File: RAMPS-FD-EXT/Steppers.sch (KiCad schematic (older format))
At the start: 20 parts, among them P401 CONN_3X2, P402 CONN_3X2, P403 MOT_0, P404 MOT_1, P405 CONN_3X2, P406 CONN_3X2, P407 MOT_3, P408 MOT_2, U401 Stepper0, U402 Stepper1, U403 Stepper3, U404 Stepper2

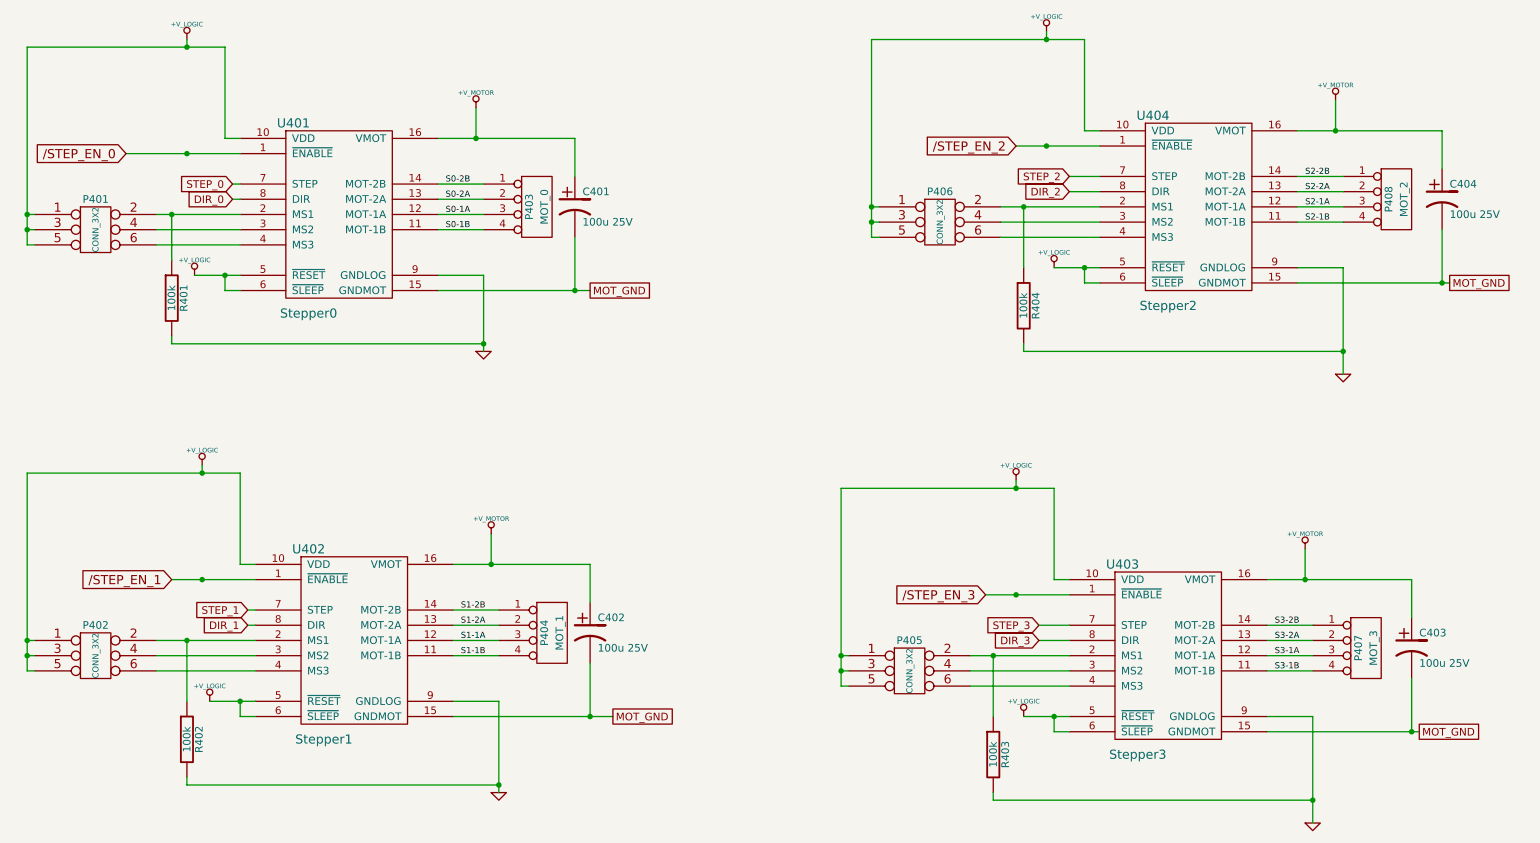
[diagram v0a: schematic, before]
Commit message: EXT4: update schematic, layout
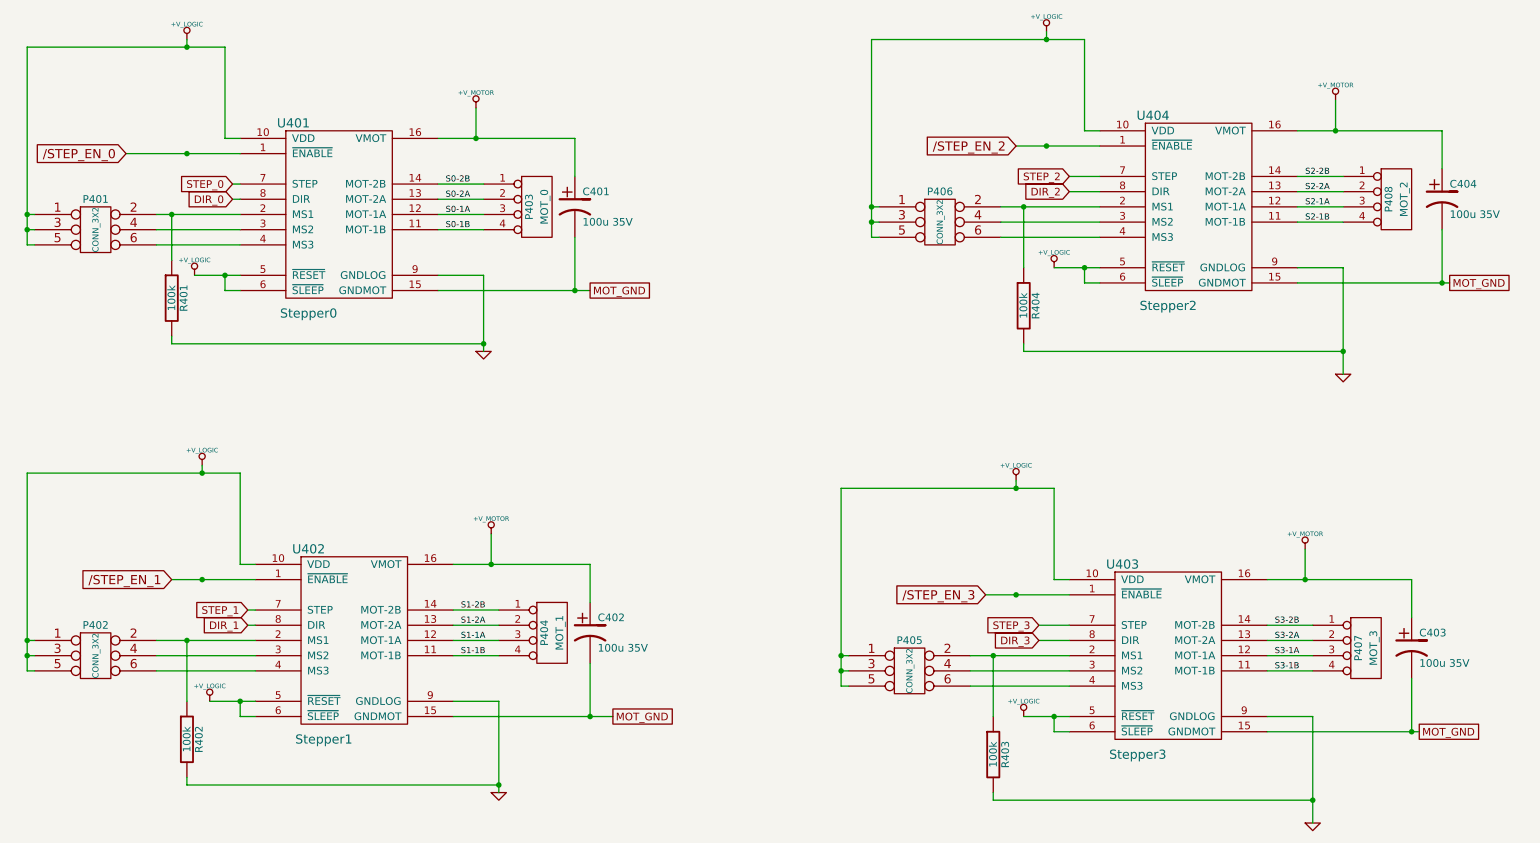
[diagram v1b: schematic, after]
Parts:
- C401, C402, C403, C404: value 100u 25V -> 100u 35V
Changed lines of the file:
@@
 Sheet 4 4
 Title ""
-Date "21 sep 2013"
+Date "26 sep 2013"
 Rev ""
 Comp ""
@@
 MOT_GND
 $Comp
-L +V_LOGIC #PWR054
+L +V_LOGIC #PWR058
 U 1 1 523B891F
 P 7500 5450
-F 0 "#PWR054" H 7500 5420 30  0001 C CNN
+F 0 "#PWR058" H 7500 5420 30  0001 C CNN
 F 1 "+V_LOGIC" H 7500 5550 30  0000 C CNN
 F 2 "" H 7500 5450 60  0001 C CNN
@@
 $EndComp
 $Comp
-L +V_LOGIC #PWR055
+L +V_LOGIC #PWR059
 U 1 1 523B891E
 P 7450 3900
-F 0 "#PWR055" H 7450 3870 30  0001 C CNN
+F 0 "#PWR059" H 7450 3870 30  0001 C CNN
 F 1 "+V_LOGIC" H 7450 4000 30  0000 C CNN
 F 2 "" H 7450 3900 60  0001 C CNN
@@
 $EndComp
 $Comp
-L +V_MOTOR #PWR056
+L +V_MOTOR #PWR060
 U 1 1 523B891D
 P 9350 4350
-F 0 "#PWR056" H 9350 4320 30  0001 C CNN
+F 0 "#PWR060" H 9350 4320 30  0001 C CNN
 F 1 "+V_MOTOR" H 9350 4450 30  0000 C CNN
 F 2 "" H 9350 4350 60  0001 C CNN
@@
 P 10050 5000
 F 0 "C403" H 10100 5100 50  0000 L CNN
-F 1 "100u 25V" H 10100 4900 50  0000 L CNN
+F 1 "100u 35V" H 10100 4900 50  0000 L CNN
 F 2 "" H 10050 5000 60  0001 C CNN
 F 3 "" H 10050 5000 60  0001 C CNN
@@
 $EndComp
 $Comp
-L GND #PWR057
+L GND #PWR061
 U 1 1 523B8918
 P 9400 6150
-F 0 "#PWR057" H 9400 6150 30  0001 C CNN
+F 0 "#PWR061" H 9400 6150 30  0001 C CNN
 F 1 "GND" H 9400 6080 30  0001 C CNN
 F 2 "" H 9400 6150 60  0001 C CNN
@@
 $EndComp
 $Comp
-L GND #PWR058
+L GND #PWR062
 U 1 1 523B869B
 P 9600 3200
-F 0 "#PWR058" H 9600 3200 30  0001 C CNN
+F 0 "#PWR062" H 9600 3200 30  0001 C CNN
 F 1 "GND" H 9600 3130 30  0001 C CNN
 F 2 "" H 9600 3200 60  0001 C CNN
@@
 P 4550 2100
 F 0 "C401" H 4600 2200 50  0000 L CNN
-F 1 "100u 25V" H 4600 2000 50  0000 L CNN
+F 1 "100u 35V" H 4600 2000 50  0000 L CNN
 F 2 "" H 4550 2100 60  0001 C CNN
 F 3 "" H 4550 2100 60  0001 C CNN
@@
 P 4650 4900
 F 0 "C402" H 4700 5000 50  0000 L CNN
-F 1 "100u 25V" H 4700 4800 50  0000 L CNN
+F 1 "100u 35V" H 4700 4800 50  0000 L CNN
 F 2 "" H 4650 4900 60  0001 C CNN
 F 3 "" H 4650 4900 60  0001 C CNN
@@
 P 10250 2050
 F 0 "C404" H 10300 2150 50  0000 L CNN
-F 1 "100u 25V" H 10300 1950 50  0000 L CNN
+F 1 "100u 35V" H 10300 1950 50  0000 L CNN
 F 2 "" H 10250 2050 60  0001 C CNN
 F 3 "" H 10250 2050 60  0001 C CNN
@@
 $EndComp
 $Comp
-L GND #PWR059
+L GND #PWR063
 U 1 1 523B8694
 P 3950 3050
-F 0 "#PWR059" H 3950 3050 30  0001 C CNN
+F 0 "#PWR063" H 3950 3050 30  0001 C CNN
 F 1 "GND" H 3950 2980 30  0001 C CNN
 F 2 "" H 3950 3050 60  0001 C CNN
@@
 $EndComp
 $Comp
-L GND #PWR060
+L GND #PWR064
 U 1 1 523B8693
 P 4050 5950
-F 0 "#PWR060" H 4050 5950 30  0001 C CNN
+F 0 "#PWR064" H 4050 5950 30  0001 C CNN
 F 1 "GND" H 4050 5880 30  0001 C CNN
 F 2 "" H 4050 5950 60  0001 C CNN
@@
 $EndComp
 $Comp
-L +V_MOTOR #PWR061
+L +V_MOTOR #PWR065
 U 1 1 523B8690
 P 3900 1450
-F 0 "#PWR061" H 3900 1420 30  0001 C CNN
+F 0 "#PWR065" H 3900 1420 30  0001 C CNN
 F 1 "+V_MOTOR" H 3900 1550 30  0000 C CNN
 F 2 "" H 3900 1450 60  0001 C CNN
@@
 $EndComp
 $Comp
-L +V_MOTOR #PWR062
+L +V_MOTOR #PWR066
 U 1 1 523B868F
 P 4000 4250
-F 0 "#PWR062" H 4000 4220 30  0001 C CNN
+F 0 "#PWR066" H 4000 4220 30  0001 C CNN
 F 1 "+V_MOTOR" H 4000 4350 30  0000 C CNN
 F 2 "" H 4000 4250 60  0001 C CNN
@@
 $EndComp
 $Comp
-L +V_MOTOR #PWR063
+L +V_MOTOR #PWR067
 U 1 1 523B868E
 P 9550 1400
-F 0 "#PWR063" H 9550 1370 30  0001 C CNN
+F 0 "#PWR067" H 9550 1370 30  0001 C CNN
 F 1 "+V_MOTOR" H 9550 1500 30  0000 C CNN
 F 2 "" H 9550 1400 60  0001 C CNN
@@
 $EndComp
 $Comp
-L +V_LOGIC #PWR064
+L +V_LOGIC #PWR068
 U 1 1 523B868D
 P 2000 1000
-F 0 "#PWR064" H 2000 970 30  0001 C CNN
+F 0 "#PWR068" H 2000 970 30  0001 C CNN
 F 1 "+V_LOGIC" H 2000 1100 30  0000 C CNN
 F 2 "" H 2000 1000 60  0001 C CNN
@@
 $EndComp
 $Comp
-L +V_LOGIC #PWR065
+L +V_LOGIC #PWR069
 U 1 1 523B868C
 P 2100 3800
-F 0 "#PWR065" H 2100 3770 30  0001 C CNN
+F 0 "#PWR069" H 2100 3770 30  0001 C CNN
 F 1 "+V_LOGIC" H 2100 3900 30  0000 C CNN
 F 2 "" H 2100 3800 60  0001 C CNN
@@
 $EndComp
 $Comp
-L +V_LOGIC #PWR066
+L +V_LOGIC #PWR070
 U 1 1 523B868B
 P 7650 950
-F 0 "#PWR066" H 7650 920 30  0001 C CNN
+F 0 "#PWR070" H 7650 920 30  0001 C CNN
 F 1 "+V_LOGIC" H 7650 1050 30  0000 C CNN
 F 2 "" H 7650 950 60  0001 C CNN
@@
 $EndComp
 $Comp
-L +V_LOGIC #PWR067
+L +V_LOGIC #PWR071
 U 1 1 523B868A
 P 2050 2550
-F 0 "#PWR067" H 2050 2520 30  0001 C CNN
+F 0 "#PWR071" H 2050 2520 30  0001 C CNN
 F 1 "+V_LOGIC" H 2050 2650 30  0000 C CNN
 F 2 "" H 2050 2550 60  0001 C CNN
@@
 $EndComp
 $Comp
-L +V_LOGIC #PWR068
+L +V_LOGIC #PWR072
 U 1 1 523B8689
 P 2150 5350
-F 0 "#PWR068" H 2150 5320 30  0001 C CNN
+F 0 "#PWR072" H 2150 5320 30  0001 C CNN
 F 1 "+V_LOGIC" H 2150 5450 30  0000 C CNN
 F 2 "" H 2150 5350 60  0001 C CNN
@@
 $EndComp
 $Comp
-L +V_LOGIC #PWR069
+L +V_LOGIC #PWR073
 U 1 1 523B8688
 P 7700 2500
-F 0 "#PWR069" H 7700 2470 30  0001 C CNN
+F 0 "#PWR073" H 7700 2470 30  0001 C CNN
 F 1 "+V_LOGIC" H 7700 2600 30  0000 C CNN
 F 2 "" H 7700 2500 60  0001 C CNN

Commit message: RAMPS-FD-EXT: update, schematic, routing and gerbers
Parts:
- P401: value CONN_3X2 -> M0
- P402: value CONN_3X2 -> M1
- P405: value CONN_3X2 -> M3
- P406: value CONN_3X2 -> M2
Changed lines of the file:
@@
 Sheet 4 4
 Title ""
-Date "26 sep 2013"
+Date "6 oct 2013"
 Rev ""
 Comp ""
@@
 MOT_GND
 $Comp
-L +V_LOGIC #PWR058
+L +V_LOGIC #PWR059
 U 1 1 523B891F
 P 7500 5450
-F 0 "#PWR058" H 7500 5420 30  0001 C CNN
+F 0 "#PWR059" H 7500 5420 30  0001 C CNN
 F 1 "+V_LOGIC" H 7500 5550 30  0000 C CNN
 F 2 "" H 7500 5450 60  0001 C CNN
@@
 $EndComp
 $Comp
-L +V_LOGIC #PWR059
+L +V_LOGIC #PWR060
 U 1 1 523B891E
 P 7450 3900
-F 0 "#PWR059" H 7450 3870 30  0001 C CNN
+F 0 "#PWR060" H 7450 3870 30  0001 C CNN
 F 1 "+V_LOGIC" H 7450 4000 30  0000 C CNN
 F 2 "" H 7450 3900 60  0001 C CNN
@@
 $EndComp
 $Comp
-L +V_MOTOR #PWR060
+L +V_MOTOR #PWR061
 U 1 1 523B891D
 P 9350 4350
-F 0 "#PWR060" H 9350 4320 30  0001 C CNN
+F 0 "#PWR061" H 9350 4320 30  0001 C CNN
 F 1 "+V_MOTOR" H 9350 4450 30  0000 C CNN
 F 2 "" H 9350 4350 60  0001 C CNN
@@
 P 6750 5200
 F 0 "P405" H 6750 5450 50  0000 C CNN
-F 1 "CONN_3X2" V 6750 5250 40  0000 C CNN
+F 1 "M3" V 6750 5250 40  0000 C CNN
 F 2 "" H 6750 5200 60  0001 C CNN
 F 3 "" H 6750 5200 60  0001 C CNN
@@
 $EndComp
 $Comp
-L GND #PWR061
+L GND #PWR062
 U 1 1 523B8918
 P 9400 6150
-F 0 "#PWR061" H 9400 6150 30  0001 C CNN
+F 0 "#PWR062" H 9400 6150 30  0001 C CNN
 F 1 "GND" H 9400 6080 30  0001 C CNN
 F 2 "" H 9400 6150 60  0001 C CNN
@@
 P 1400 2300
 F 0 "P401" H 1400 2550 50  0000 C CNN
-F 1 "CONN_3X2" V 1400 2350 40  0000 C CNN
+F 1 "M0" V 1400 2350 40  0000 C CNN
 F 2 "" H 1400 2300 60  0001 C CNN
 F 3 "" H 1400 2300 60  0001 C CNN
@@
 P 1400 5100
 F 0 "P402" H 1400 5350 50  0000 C CNN
-F 1 "CONN_3X2" V 1400 5150 40  0000 C CNN
+F 1 "M1" V 1400 5150 40  0000 C CNN
 F 2 "" H 1400 5100 60  0001 C CNN
 F 3 "" H 1400 5100 60  0001 C CNN
@@
 $EndComp
 $Comp
-L GND #PWR062
+L GND #PWR063
 U 1 1 523B869B
 P 9600 3200
-F 0 "#PWR062" H 9600 3200 30  0001 C CNN
+F 0 "#PWR063" H 9600 3200 30  0001 C CNN
 F 1 "GND" H 9600 3130 30  0001 C CNN
 F 2 "" H 9600 3200 60  0001 C CNN
@@
 P 6950 2250
 F 0 "P406" H 6950 2500 50  0000 C CNN
-F 1 "CONN_3X2" V 6950 2300 40  0000 C CNN
+F 1 "M2" V 6950 2300 40  0000 C CNN
 F 2 "" H 6950 2250 60  0001 C CNN
 F 3 "" H 6950 2250 60  0001 C CNN
@@
 $EndComp
 $Comp
-L GND #PWR063
+L GND #PWR064
 U 1 1 523B8694
 P 3950 3050
-F 0 "#PWR063" H 3950 3050 30  0001 C CNN
+F 0 "#PWR064" H 3950 3050 30  0001 C CNN
 F 1 "GND" H 3950 2980 30  0001 C CNN
 F 2 "" H 3950 3050 60  0001 C CNN
@@
 $EndComp
 $Comp
-L GND #PWR064
+L GND #PWR065
 U 1 1 523B8693
 P 4050 5950
-F 0 "#PWR064" H 4050 5950 30  0001 C CNN
+F 0 "#PWR065" H 4050 5950 30  0001 C CNN
 F 1 "GND" H 4050 5880 30  0001 C CNN
 F 2 "" H 4050 5950 60  0001 C CNN
@@
 $EndComp
 $Comp
-L +V_MOTOR #PWR065
+L +V_MOTOR #PWR066
 U 1 1 523B8690
 P 3900 1450
-F 0 "#PWR065" H 3900 1420 30  0001 C CNN
+F 0 "#PWR066" H 3900 1420 30  0001 C CNN
 F 1 "+V_MOTOR" H 3900 1550 30  0000 C CNN
 F 2 "" H 3900 1450 60  0001 C CNN
@@
 $EndComp
 $Comp
-L +V_MOTOR #PWR066
+L +V_MOTOR #PWR067
 U 1 1 523B868F
 P 4000 4250
-F 0 "#PWR066" H 4000 4220 30  0001 C CNN
+F 0 "#PWR067" H 4000 4220 30  0001 C CNN
 F 1 "+V_MOTOR" H 4000 4350 30  0000 C CNN
 F 2 "" H 4000 4250 60  0001 C CNN
@@
 $EndComp
 $Comp
-L +V_MOTOR #PWR067
+L +V_MOTOR #PWR068
 U 1 1 523B868E
 P 9550 1400
-F 0 "#PWR067" H 9550 1370 30  0001 C CNN
+F 0 "#PWR068" H 9550 1370 30  0001 C CNN
 F 1 "+V_MOTOR" H 9550 1500 30  0000 C CNN
 F 2 "" H 9550 1400 60  0001 C CNN
@@
 $EndComp
 $Comp
-L +V_LOGIC #PWR068
+L +V_LOGIC #PWR069
 U 1 1 523B868D
 P 2000 1000
-F 0 "#PWR068" H 2000 970 30  0001 C CNN
+F 0 "#PWR069" H 2000 970 30  0001 C CNN
 F 1 "+V_LOGIC" H 2000 1100 30  0000 C CNN
 F 2 "" H 2000 1000 60  0001 C CNN
@@
 $EndComp
 $Comp
-L +V_LOGIC #PWR069
+L +V_LOGIC #PWR070
 U 1 1 523B868C
 P 2100 3800
-F 0 "#PWR069" H 2100 3770 30  0001 C CNN
+F 0 "#PWR070" H 2100 3770 30  0001 C CNN
 F 1 "+V_LOGIC" H 2100 3900 30  0000 C CNN
 F 2 "" H 2100 3800 60  0001 C CNN
@@
 $EndComp
 $Comp
-L +V_LOGIC #PWR070
+L +V_LOGIC #PWR071
 U 1 1 523B868B
 P 7650 950
-F 0 "#PWR070" H 7650 920 30  0001 C CNN
+F 0 "#PWR071" H 7650 920 30  0001 C CNN
 F 1 "+V_LOGIC" H 7650 1050 30  0000 C CNN
 F 2 "" H 7650 950 60  0001 C CNN
@@
 $EndComp
 $Comp
-L +V_LOGIC #PWR071
+L +V_LOGIC #PWR072
 U 1 1 523B868A
 P 2050 2550
-F 0 "#PWR071" H 2050 2520 30  0001 C CNN
+F 0 "#PWR072" H 2050 2520 30  0001 C CNN
 F 1 "+V_LOGIC" H 2050 2650 30  0000 C CNN
 F 2 "" H 2050 2550 60  0001 C CNN
@@
 $EndComp
 $Comp
-L +V_LOGIC #PWR072
+L +V_LOGIC #PWR073
 U 1 1 523B8689
 P 2150 5350
-F 0 "#PWR072" H 2150 5320 30  0001 C CNN
+F 0 "#PWR073" H 2150 5320 30  0001 C CNN
 F 1 "+V_LOGIC" H 2150 5450 30  0000 C CNN
 F 2 "" H 2150 5350 60  0001 C CNN
@@
 $EndComp
 $Comp
-L +V_LOGIC #PWR073
+L +V_LOGIC #PWR074
 U 1 1 523B8688
 P 7700 2500
-F 0 "#PWR073" H 7700 2470 30  0001 C CNN
+F 0 "#PWR074" H 7700 2470 30  0001 C CNN
 F 1 "+V_LOGIC" H 7700 2600 30  0000 C CNN
 F 2 "" H 7700 2500 60  0001 C CNN
